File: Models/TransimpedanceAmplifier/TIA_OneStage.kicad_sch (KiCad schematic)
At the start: 7 parts, among them J5 Conn_01x02_Pin, J6 Conn_01x02_Pin, U4 OPA828

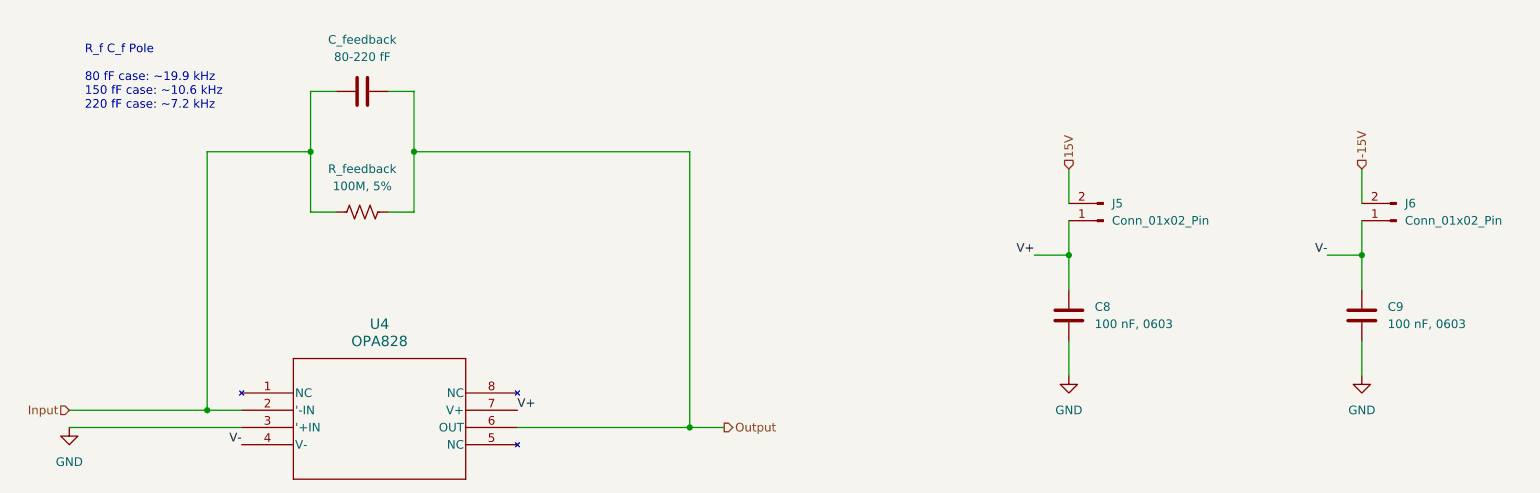
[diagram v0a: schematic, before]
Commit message: Overhauled all of the annotations
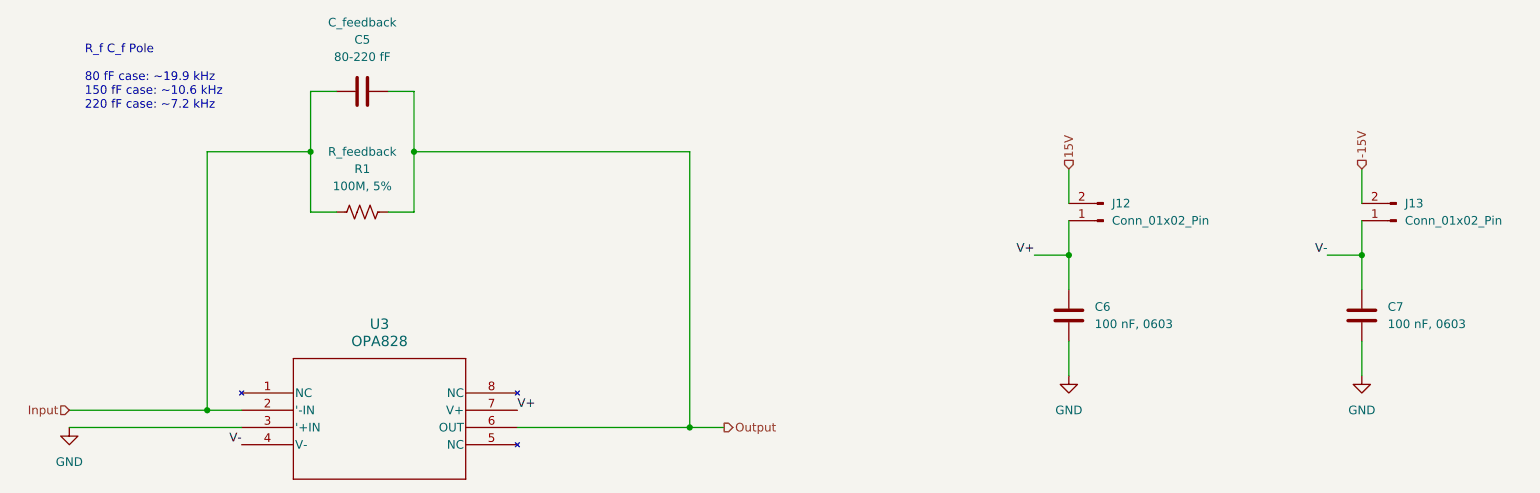
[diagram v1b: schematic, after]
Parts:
- renumbered C_feedback to C5, C8 to C6, C9 to C7, J5 to J12, J6 to J13, R_feedback to R1, U4 to U3
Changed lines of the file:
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@@
 		(dnp no)
 		(fields_autoplaced yes)
-		(property "Reference" "U4"
+		(property "Reference" "U3"
 			(at 99.06 83.82 0)
 			(effects
@@
 			(project ""
 				(path "/ec9f2ae3-e40d-40eb-9760-2b611ee8efd1/f970a304-10fa-492d-98c3-214694e65338"
-					(reference "U4")
+					(reference "U3")
 					(unit 1)
 				)
@@
 		(on_board no)
 		(dnp no)
-		(fields_autoplaced yes)
-		(property "Reference" "C_feedback"
+		(property "Reference" "C5"
 			(at 96.52 41.91 90)
 			(effects
@@
 			)
 		)
-		(property "Description" "Unpolarized capacitor"
-			(at 96.52 49.53 0)
-			(effects
-				(font
-					(size 1.27 1.27)
-				)
-				(hide yes)
+		(property "Description" "C_feedback"
+			(at 96.52 39.37 90)
+			(effects
+				(font
+					(size 1.27 1.27)
+				)
 			)
 		)
@@
 			(project "TransimpedanceAmplifier"
 				(path "/ec9f2ae3-e40d-40eb-9760-2b611ee8efd1/f970a304-10fa-492d-98c3-214694e65338"
-					(reference "C_feedback")
+					(reference "C5")
 					(unit 1)
 				)
@@
 		(on_board yes)
 		(dnp no)
-		(fields_autoplaced yes)
-		(property "Reference" "R_feedback"
+		(property "Reference" "R1"
 			(at 96.52 60.96 90)
 			(effects
@@
 			)
 		)
-		(property "Description" "Resistor, US symbol"
-			(at 96.52 67.31 0)
-			(effects
-				(font
-					(size 1.27 1.27)
-				)
-				(hide yes)
+		(property "Description" "R_feedback"
+			(at 96.52 58.42 90)
+			(effects
+				(font
+					(size 1.27 1.27)
+				)
 			)
 		)
@@
 			(project ""
 				(path "/ec9f2ae3-e40d-40eb-9760-2b611ee8efd1/f970a304-10fa-492d-98c3-214694e65338"
-					(reference "R_feedback")
+					(reference "R1")
 					(unit 1)
 				)
@@
 		(dnp no)
 		(fields_autoplaced yes)
-		(property "Reference" "J6"
+		(property "Reference" "J13"
 			(at 250.19 66.0399 0)
 			(effects
@@
 			(project "TransimpedanceAmplifier"
 				(path "/ec9f2ae3-e40d-40eb-9760-2b611ee8efd1/f970a304-10fa-492d-98c3-214694e65338"
-					(reference "J6")
+					(reference "J13")
 					(unit 1)
 				)
@@
 		(dnp no)
 		(fields_autoplaced yes)
-		(property "Reference" "C8"
+		(property "Reference" "C6"
 			(at 204.47 81.2799 0)
 			(effects
@@
 			(project ""
 				(path "/ec9f2ae3-e40d-40eb-9760-2b611ee8efd1/f970a304-10fa-492d-98c3-214694e65338"
-					(reference "C8")
+					(reference "C6")
 					(unit 1)
 				)
@@
 		(dnp no)
 		(fields_autoplaced yes)
-		(property "Reference" "#PWR03"
+		(property "Reference" "#PWR013"
 			(at 200.66 97.79 0)
 			(effects
@@
 			(project "TransimpedanceAmplifier"
 				(path "/ec9f2ae3-e40d-40eb-9760-2b611ee8efd1/f970a304-10fa-492d-98c3-214694e65338"
-					(reference "#PWR03")
+					(reference "#PWR013")
 					(unit 1)
 				)
@@
 		(dnp no)
 		(fields_autoplaced yes)
-		(property "Reference" "#PWR024"
+		(property "Reference" "#PWR012"
 			(at 53.34 105.41 0)
 			(effects
@@
 			(project ""
 				(path "/ec9f2ae3-e40d-40eb-9760-2b611ee8efd1/f970a304-10fa-492d-98c3-214694e65338"
-					(reference "#PWR024")
+					(reference "#PWR012")
 					(unit 1)
 				)
@@
 		(dnp no)
 		(fields_autoplaced yes)
-		(property "Reference" "#PWR023"
+		(property "Reference" "#PWR014"
 			(at 243.84 97.79 0)
 			(effects
@@
 			(project "TransimpedanceAmplifier"
 				(path "/ec9f2ae3-e40d-40eb-9760-2b611ee8efd1/f970a304-10fa-492d-98c3-214694e65338"
-					(reference "#PWR023")
+					(reference "#PWR014")
 					(unit 1)
 				)
@@
 		(dnp no)
 		(fields_autoplaced yes)
-		(property "Reference" "J5"
+		(property "Reference" "J12"
 			(at 207.01 66.0399 0)
 			(effects
@@
 			(project ""
 				(path "/ec9f2ae3-e40d-40eb-9760-2b611ee8efd1/f970a304-10fa-492d-98c3-214694e65338"
-					(reference "J5")
+					(reference "J12")
 					(unit 1)
 				)
@@
 		(dnp no)
 		(fields_autoplaced yes)
-		(property "Reference" "C9"
+		(property "Reference" "C7"
 			(at 247.65 81.2799 0)
 			(effects
@@
 			(project "TransimpedanceAmplifier"
 				(path "/ec9f2ae3-e40d-40eb-9760-2b611ee8efd1/f970a304-10fa-492d-98c3-214694e65338"
-					(reference "C9")
-					(unit 1)
-				)
+					(reference "C7")
+					(unit 1)
+				)

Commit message: Completely fixed the batteries
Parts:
- renumbered J12 to J4, J13 to J5
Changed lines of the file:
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@@
 		(dnp no)
 		(fields_autoplaced yes)
-		(property "Reference" "J13"
+		(property "Reference" "J5"
 			(at 250.19 66.0399 0)
 			(effects
@@
 			(project "TransimpedanceAmplifier"
 				(path "/ec9f2ae3-e40d-40eb-9760-2b611ee8efd1/f970a304-10fa-492d-98c3-214694e65338"
-					(reference "J13")
+					(reference "J5")
 					(unit 1)
 				)
@@
 		(dnp no)
 		(fields_autoplaced yes)
-		(property "Reference" "J12"
+		(property "Reference" "J4"
 			(at 207.01 66.0399 0)
 			(effects
@@
 			(project ""
 				(path "/ec9f2ae3-e40d-40eb-9760-2b611ee8efd1/f970a304-10fa-492d-98c3-214694e65338"
-					(reference "J12")
-					(unit 1)
-				)
+					(reference "J4")
+					(unit 1)
+				)

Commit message: Finalized the last detail of the schematic
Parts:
- renumbered R1 to R2
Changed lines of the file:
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@@
 		(on_board yes)
 		(dnp no)
-		(property "Reference" "R1"
+		(property "Reference" "R2"
 			(at 96.52 60.96 90)
 			(effects
@@
 			(project ""
 				(path "/ec9f2ae3-e40d-40eb-9760-2b611ee8efd1/f970a304-10fa-492d-98c3-214694e65338"
-					(reference "R1")
+					(reference "R2")
 					(unit 1)
 				)

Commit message: Working on filling in the last details of the schematics
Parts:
- C5, R2, U3: Cost (none) -> $0.00; RoHS Compliant (none) -> NO
- C6, C7: footprint (none) -> TwoTerminal:CAPC0603; Cost (none) -> $0.00; RoHS Compliant (none) -> NO
- J4, J5: footprint (none) -> Connector_Custom:PinHeader_1x2; Cost (none) -> $0.00; RoHS Compliant (none) -> NO
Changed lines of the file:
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@@
+			)
+		)
+		(property "Cost" "$0.00"
+			(at 78.74 93.98 0)
+			(effects
+				(font
+					(size 1.27 1.27)
+				)
+				(hide yes)
+			)
+		)
+		(property "RoHS Compliant" "NO"
+			(at 78.74 93.98 0)
+			(effects
+				(font
+					(size 1.27 1.27)
+				)
+				(hide yes)
 			)
 		)
@@
 			)
 		)
+		(property "Cost" "$0.00"
+			(at 96.52 49.53 90)
+			(effects
+				(font
+					(size 1.27 1.27)
+				)
+				(hide yes)
+			)
+		)
+		(property "RoHS Compliant" "NO"
+			(at 96.52 49.53 90)
+			(effects
+				(font
+					(size 1.27 1.27)
+				)
+				(hide yes)
+			)
+		)
 		(pin "2"
 		)
@@
 		(property "Purchase Link" "https://www.digikey.com/en/products/detail/vishay-dale/CRCW0805100MJPEAHR/3232302"
 			(at 96.52 67.31 0)
+			(effects
+				(font
+					(size 1.27 1.27)
+				)
+				(hide yes)
+			)
+		)
+		(property "Cost" "$0.00"
+			(at 96.52 67.31 90)
+			(effects
+				(font
+					(size 1.27 1.27)
+				)
+				(hide yes)
+			)
+		)
+		(property "RoHS Compliant" "NO"
+			(at 96.52 67.31 90)
 			(effects
 				(font
@@
 			)
 		)
-		(property "Footprint" ""
+		(property "Footprint" "Connector_Custom:PinHeader_1x2"
 			(at 248.92 68.58 0)
 			(effects
@@
 		)
 		(property "Purchase Link" "https://www.digikey.com/en/products/detail/sullins-connector-solutions/QPC02SXGN-RC/2618262"
+			(at 248.92 68.58 0)
+			(effects
+				(font
+					(size 1.27 1.27)
+				)
+				(hide yes)
+			)
+		)
+		(property "Cost" "$0.00"
+			(at 248.92 68.58 0)
+			(effects
+				(font
+					(size 1.27 1.27)
+				)
+				(hide yes)
+			)
+		)
+		(property "RoHS Compliant" "NO"
 			(at 248.92 68.58 0)
 			(effects
@@
 			)
 		)
-		(property "Footprint" ""
+		(property "Footprint" "TwoTerminal:CAPC0603"
 			(at 201.6252 86.36 0)
 			(effects
@@
 		)
 		(property "Purchase Link" "https://www.digikey.com/en/products/detail/murata-electronics/GRM188R72A104KA35D/702549"
+			(at 200.66 82.55 0)
+			(effects
+				(font
+					(size 1.27 1.27)
+				)
+				(hide yes)
+			)
+		)
+		(property "Cost" "$0.00"
+			(at 200.66 82.55 0)
+			(effects
+				(font
+					(size 1.27 1.27)
+				)
+				(hide yes)
+			)
+		)
+		(property "RoHS Compliant" "NO"
 			(at 200.66 82.55 0)
 			(effects
@@
 			)
 		)
-		(property "Footprint" ""
+		(property "Footprint" "Connector_Custom:PinHeader_1x2"
 			(at 205.74 68.58 0)
 			(effects
@@
 		)
 		(property "Purchase Link" "https://www.digikey.com/en/products/detail/sullins-connector-solutions/QPC02SXGN-RC/2618262"
+			(at 205.74 68.58 0)
+			(effects
+				(font
+					(size 1.27 1.27)
+				)
+				(hide yes)
+			)
+		)
+		(property "Cost" "$0.00"
+			(at 205.74 68.58 0)
+			(effects
+				(font
+					(size 1.27 1.27)
+				)
+				(hide yes)
+			)
+		)
+		(property "RoHS Compliant" "NO"
 			(at 205.74 68.58 0)
 			(effects
@@
 			)
 		)
-		(property "Footprint" ""
+		(property "Footprint" "TwoTerminal:CAPC0603"
 			(at 244.8052 86.36 0)
 			(effects
@@
 			(at 243.84 82.55 0)
 			(effects
+				(font
+					(size 1.27 1.27)
+				)
+				(hide yes)
+			)
+		)
+		(property "Cost" "$0.00"
+			(at 243.84 82.55 0)
+			(effects
+				(font
+					(size 1.27 1.27)
+				)
+				(hide yes)
+			)
+		)
+		(property "RoHS Compliant" "NO"
+			(at 243.84 82.55 0)
+			(effects

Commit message: Fixed a bug in footprint assignment
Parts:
- R2: footprint (none) -> TwoTerminal:RESC0805
- U3: footprint (none) -> IC:SOIC-8
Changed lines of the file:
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@@
 			)
 		)
-		(property "Footprint" ""
+		(property "Footprint" "IC:SOIC-8"
 			(at 78.74 93.98 0)
 			(effects
@@
 			)
 		)
-		(property "Footprint" ""
+		(property "Footprint" "TwoTerminal:RESC0805"
 			(at 96.774 66.294 90)
 			(effects

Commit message: Save progress
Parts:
- C5: Cost $0.00 -> (none); RoHS Compliant NO -> (none)
- C6, C7: Cost $0.00 -> $0.15; Cost (qty10) (none) -> $0.087; RoHS Compliant NO -> YES
- J4, J5: Cost $0.00 -> $0.10; Cost (qty10) (none) -> $0.025; RoHS Compliant NO -> YES
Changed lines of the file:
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@@
 			)
 		)
-		(property "Cost" "$0.00"
+		(property "Cost" ""
 			(at 96.52 49.53 90)
 			(effects
@@
 			)
 		)
-		(property "RoHS Compliant" "NO"
+		(property "RoHS Compliant" ""
 			(at 96.52 49.53 90)
 			(effects
@@
 			)
 		)
-		(property "Cost" "$0.00"
+		(property "Cost" "$0.10"
 			(at 248.92 68.58 0)
 			(effects
@@
 			)
 		)
-		(property "RoHS Compliant" "NO"
+		(property "RoHS Compliant" "YES"
+			(at 248.92 68.58 0)
+			(effects
+				(font
+					(size 1.27 1.27)
+				)
+				(hide yes)
+			)
+		)
+		(property "Cost (qty10)" "$0.025"
 			(at 248.92 68.58 0)
 			(effects
@@
 			)
 		)
-		(property "Cost" "$0.00"
+		(property "Cost" "$0.15"
 			(at 200.66 82.55 0)
 			(effects
@@
 			)
 		)
-		(property "RoHS Compliant" "NO"
+		(property "RoHS Compliant" "YES"
+			(at 200.66 82.55 0)
+			(effects
+				(font
+					(size 1.27 1.27)
+				)
+				(hide yes)
+			)
+		)
+		(property "Cost (qty10)" "$0.087"
 			(at 200.66 82.55 0)
 			(effects
@@
 			)
 		)
-		(property "Cost" "$0.00"
+		(property "Cost" "$0.10"
 			(at 205.74 68.58 0)
 			(effects
@@
 			)
 		)
-		(property "RoHS Compliant" "NO"
+		(property "RoHS Compliant" "YES"
+			(at 205.74 68.58 0)
+			(effects
+				(font
+					(size 1.27 1.27)
+				)
+				(hide yes)
+			)
+		)
+		(property "Cost (qty10)" "$0.025"
 			(at 205.74 68.58 0)
 			(effects
@@
 			)
 		)
-		(property "Cost" "$0.00"
+		(property "Cost" "$0.15"
 			(at 243.84 82.55 0)
 			(effects
@@
 			)
 		)
-		(property "RoHS Compliant" "NO"
+		(property "RoHS Compliant" "YES"
 			(at 243.84 82.55 0)
 			(effects
+				(font
+					(size 1.27 1.27)
+				)
+				(hide yes)
+			)
+		)
+		(property "Cost (qty10)" "$0.087"
+			(at 243.84 82.55 0)
+			(effects

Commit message: Added important links regarding high-voltage electronics
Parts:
- R2: Cost $0.00 -> $0.38; Cost (qty10) (none) -> $0.213; RoHS Compliant NO -> YES
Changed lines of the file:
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@@
 			)
 		)
-		(property "Cost" "$0.00"
+		(property "Cost" "$0.38"
 			(at 96.52 67.31 90)
 			(effects
@@
 			)
 		)
-		(property "RoHS Compliant" "NO"
+		(property "RoHS Compliant" "YES"
 			(at 96.52 67.31 90)
 			(effects
+				(font
+					(size 1.27 1.27)
+				)
+				(hide yes)
+			)
+		)
+		(property "Cost (qty10)" "$0.213"
+			(at 96.52 67.31 90)
+			(effects

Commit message: Starting major changes in response to the SOIC-8 version of OP37 being out of stock
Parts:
- U3: Cost $0.00 -> $7.50; Cost (qty10) (none) -> $5.78; Purchase Link https://www.digikey.com/en/products/detail/texas-instrument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 -> https://www.mouser.com/ProductDetail/Texas-Instruments/OPA8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; RoHS Compliant NO -> YES
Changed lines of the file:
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@@
 			)
 		)
-		(property "Purchase Link" "https://www.digikey.com/en/products/detail/texas-instruments/OPA828IDR/10820196"
+		(property "Purchase Link" "https://www.mouser.com/ProductDetail/Texas-Instruments/OPA828IDR?qs=qSfuJ%252Bfl%2Fd4dEw5JbvByEQ%3D%3D"
 			(at 78.74 93.98 0)
 			(effects
@@
 			)
 		)
-		(property "Cost" "$0.00"
+		(property "Cost" "$7.50"
 			(at 78.74 93.98 0)
 			(effects
@@
 			)
 		)
-		(property "RoHS Compliant" "NO"
+		(property "RoHS Compliant" "YES"
 			(at 78.74 93.98 0)
 			(effects
+				(font
+					(size 1.27 1.27)
+				)
+				(hide yes)
+			)
+		)
+		(property "Cost (qty10)" "$5.78"
+			(at 78.74 93.98 0)
+			(effects
